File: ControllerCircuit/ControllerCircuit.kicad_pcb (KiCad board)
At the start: 2 copper layers, 122.5 x 87.5 mm, 87 parts, among them J1 ScrewTerminal, J10 Conn_01x02_Female, J11 Conn_01x03_Female, J12 ScrewTerminal, J13 Conn_01x02_Female, J14 ScrewTerminal, J15 Molex 0472192001, J2 ScrewTerminal3Pin, J3 ScrewTerminal3Pin, J4 ScrewTerminal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

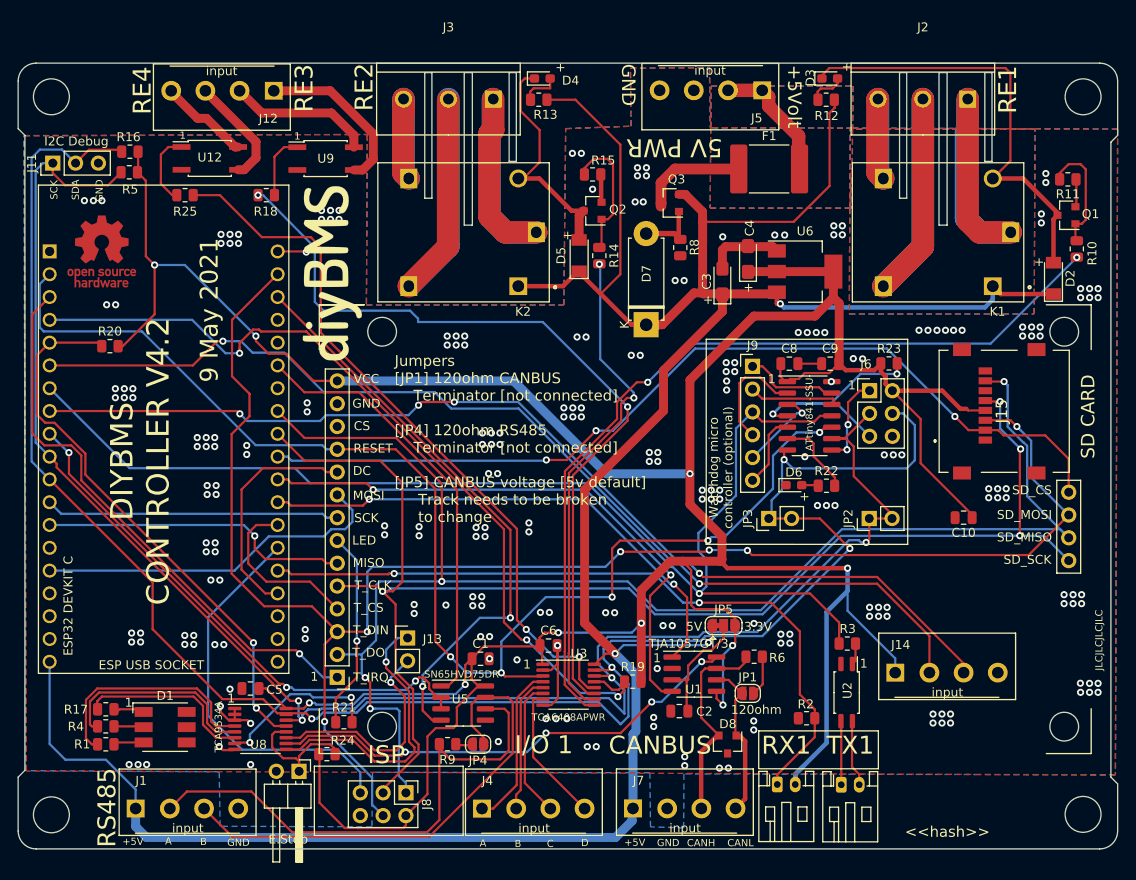
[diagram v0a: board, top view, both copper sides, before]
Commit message: More kicad6 migration
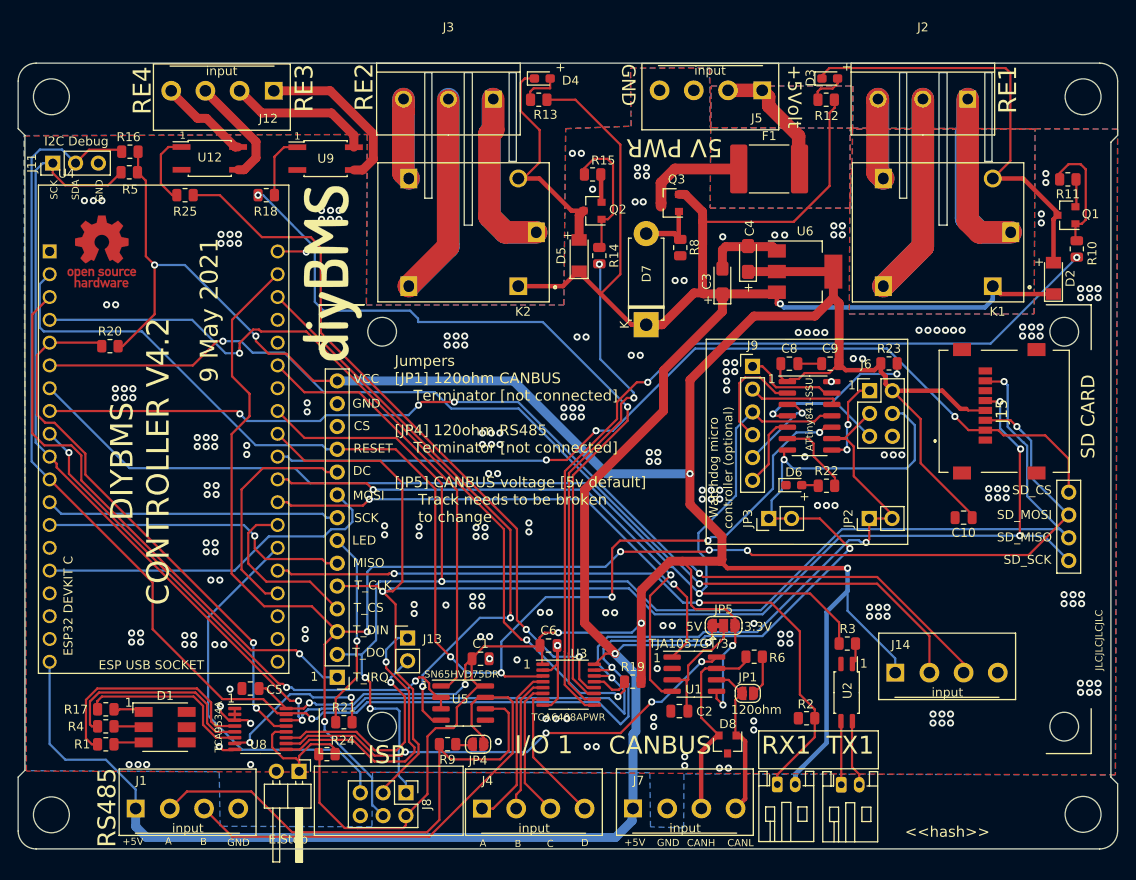
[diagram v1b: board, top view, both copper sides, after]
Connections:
- J15 pad 1: (no net) -> unconnected-(J15-Pad1)
- J15 pad 8: (no net) -> unconnected-(J15-Pad8)
- U4 pad 1: (no net) -> /ESP3V3
- U4 pad 16: (no net) -> unconnected-(U4-Pad16)
- U4 pad 17: (no net) -> unconnected-(U4-Pad17)
- U4 pad 18: (no net) -> unconnected-(U4-Pad18)
- U4 pad 23: (no net) -> unconnected-(U4-Pad23)
- U4 pad 24: (no net) -> unconnected-(U4-Pad24)
- U4 pad 36: (no net) -> unconnected-(U4-Pad36)
- U4 pad 37: (no net) -> unconnected-(U4-Pad37)
- U4 pad 38: (no net) -> unconnected-(U4-Pad38)
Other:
- net class Default removed
- net class Half mm removed
- net class High Clearance removed
- net class Relay removed
